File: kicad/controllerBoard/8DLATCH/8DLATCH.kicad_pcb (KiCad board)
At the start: 2 copper layers, 96 parts, among them Q1 Q_PMOS_GSD, Q10 Q_NMOS_GSD, Q11 Q_PMOS_GSD, Q12 Q_NMOS_GSD, Q13 Q_PMOS_GSD, Q14 Q_NMOS_GSD, Q15 Q_PMOS_GSD, Q16 Q_NMOS_GSD, Q17 Q_PMOS_GSD, Q18 Q_NMOS_GSD, Q19 Q_PMOS_GSD, Q2 Q_NMOS_GSD, Q20 Q_NMOS_GSD, Q21 Q_PMOS_GSD, Q22 Q_NMOS_GSD, Q23 Q_PMOS_GSD, Q24 Q_NMOS_GSD, Q25 Q_PMOS_GSD, Q26 Q_NMOS_GSD, Q27 Q_PMOS_GSD, Q28 Q_NMOS_GSD, Q29 Q_PMOS_GSD, Q3 Q_PMOS_GSD, Q30 Q_NMOS_GSD, Q31 Q_PMOS_GSD, Q32 Q_NMOS_GSD, Q33 Q_PMOS_GSD, Q34 Q_NMOS_GSD, Q35 Q_PMOS_GSD, Q36 Q_NMOS_GSD, Q37 Q_PMOS_GSD, Q38 Q_NMOS_GSD, Q39 Q_PMOS_GSD, Q4 Q_NMOS_GSD, Q40 Q_NMOS_GSD, Q41 Q_PMOS_GSD, Q42 Q_NMOS_GSD, Q43 Q_PMOS_GSD, Q44 Q_NMOS_GSD, Q45 Q_PMOS_GSD, Q46 Q_NMOS_GSD, Q47 Q_PMOS_GSD, Q48 Q_NMOS_GSD, Q49 Q_PMOS_GSD, Q5 Q_PMOS_GSD, Q50 Q_NMOS_GSD, Q51 Q_PMOS_GSD, Q52 Q_NMOS_GSD, Q53 Q_PMOS_GSD, Q54 Q_NMOS_GSD, Q55 Q_PMOS_GSD, Q56 Q_NMOS_GSD, Q57 Q_PMOS_GSD, Q58 Q_NMOS_GSD, Q59 Q_PMOS_GSD, Q6 Q_NMOS_GSD, Q60 Q_NMOS_GSD, Q61 Q_PMOS_GSD, Q62 Q_NMOS_GSD, Q63 Q_PMOS_GSD, Q64 Q_NMOS_GSD, Q65 Q_PMOS_GSD, Q66 Q_NMOS_GSD, Q67 Q_PMOS_GSD, Q68 Q_NMOS_GSD, Q69 Q_PMOS_GSD, Q7 Q_PMOS_GSD, Q70 Q_NMOS_GSD, Q71 Q_PMOS_GSD, Q72 Q_NMOS_GSD, Q73 Q_PMOS_GSD, Q74 Q_NMOS_GSD, Q75 Q_PMOS_GSD, Q76 Q_NMOS_GSD, Q77 Q_PMOS_GSD, Q78 Q_NMOS_GSD, Q79 Q_PMOS_GSD, Q8 Q_NMOS_GSD, Q80 Q_NMOS_GSD, Q81 Q_PMOS_GSD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

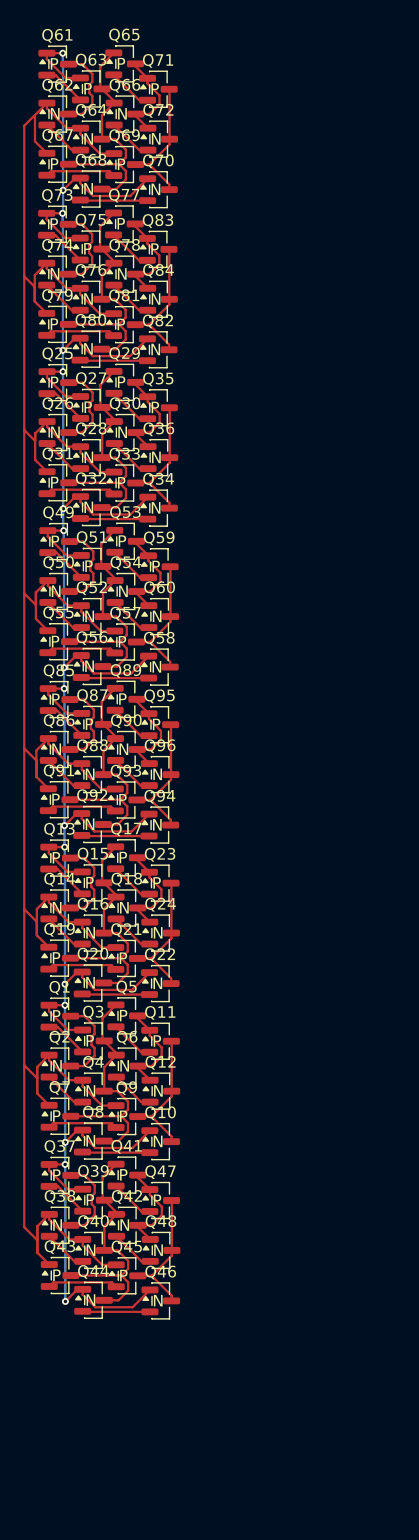
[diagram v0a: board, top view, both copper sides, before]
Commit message: add mounting holes
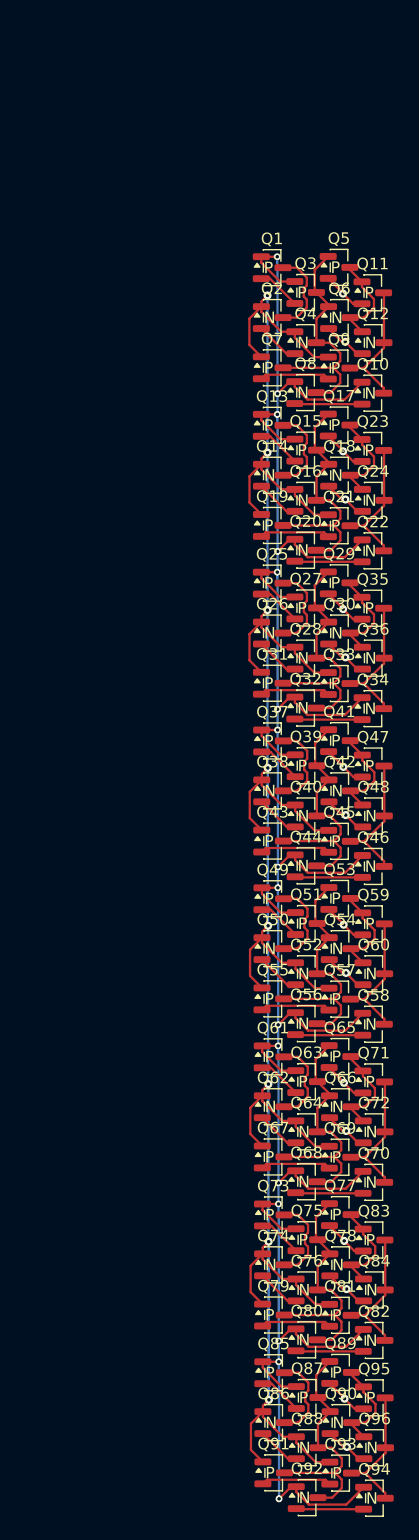
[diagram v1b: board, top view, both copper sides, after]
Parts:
- moved Q61 88.0 mm to (92.4, 118.7)
- moved Q62 88.0 mm to (92.4, 123.0)
- moved Q64 88.0 mm to (95.3, 125.2)
- moved Q65 88.0 mm to (98.2, 118.7)
- moved Q66 88.0 mm to (98.2, 123.0)
- moved Q67 88.0 mm to (92.4, 127.4)
- moved Q68 88.0 mm to (95.3, 129.5)
- moved Q69 88.0 mm to (98.2, 127.4)
- moved Q71 88.0 mm to (101.1, 120.9)
- moved Q72 88.0 mm to (101.1, 125.2)
- moved Q63 88.0 mm to (95.3, 120.8)
- moved Q70 88.0 mm to (101.1, 129.6)
- moved Q73 87.9 mm to (92.4, 132.4)
- moved Q75 87.9 mm to (95.3, 134.6)
- moved Q76 87.9 mm to (95.3, 138.9)
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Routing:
- net /EN: track 224.3 -> 212.8 mm, vias 0 -> 8
- net /~{EN}: track 226.5 -> 225.9 mm
- net Net-(Q77-S): track 3.84 -> 3.86 mm, vias 0 -> 1
- net Net-(Q29-S): track 3.84 -> 3.86 mm, vias 0 -> 1
- net Net-(Q17-S): track 3.84 -> 3.86 mm, vias 0 -> 1
- net Net-(Q89-S): track 3.84 -> 3.86 mm, vias 0 -> 1
- net Net-(Q41-S): track 3.84 -> 3.86 mm, vias 0 -> 1
- net Net-(Q65-S): track 3.84 -> 3.86 mm, vias 0 -> 1
- net Net-(Q53-S): track 3.84 -> 3.86 mm, vias 0 -> 1
- net Net-(Q11-S): track 3.84 -> 3.86 mm, vias 0 -> 1
- net Net-(Q90-S): vias 0 -> 1
- net Net-(Q18-S): vias 0 -> 1
- net Net-(Q30-S): vias 0 -> 1
- net Net-(Q78-S): vias 0 -> 1
- net Net-(Q66-S): vias 0 -> 1
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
